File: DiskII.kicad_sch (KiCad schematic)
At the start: 31 parts, among them J1 Apple II Expansion Bus, J2 DRIVE 2, J3 DRIVE 1, Q1 2N3906, Q2 MPSU51, Q3 MPSU51, SW1 A8, SW2 A9, SW3 A10

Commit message: update BOM
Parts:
- J1: now left out of the parts list
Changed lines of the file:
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@@
   )
   (symbol (lib_id "Connector_Generic:Conn_02x25_Counter_Clockwise") (at 64.77 181.61 0) (unit 1)
-    (in_bom yes) (on_board yes)
+    (in_bom no) (on_board yes)
     (property "Reference" "J1" (id 0) (at 66.04 145.6182 0))
     (property "Value" "Apple II Expansion Bus" (id 1) (at 66.04 147.9296 0))

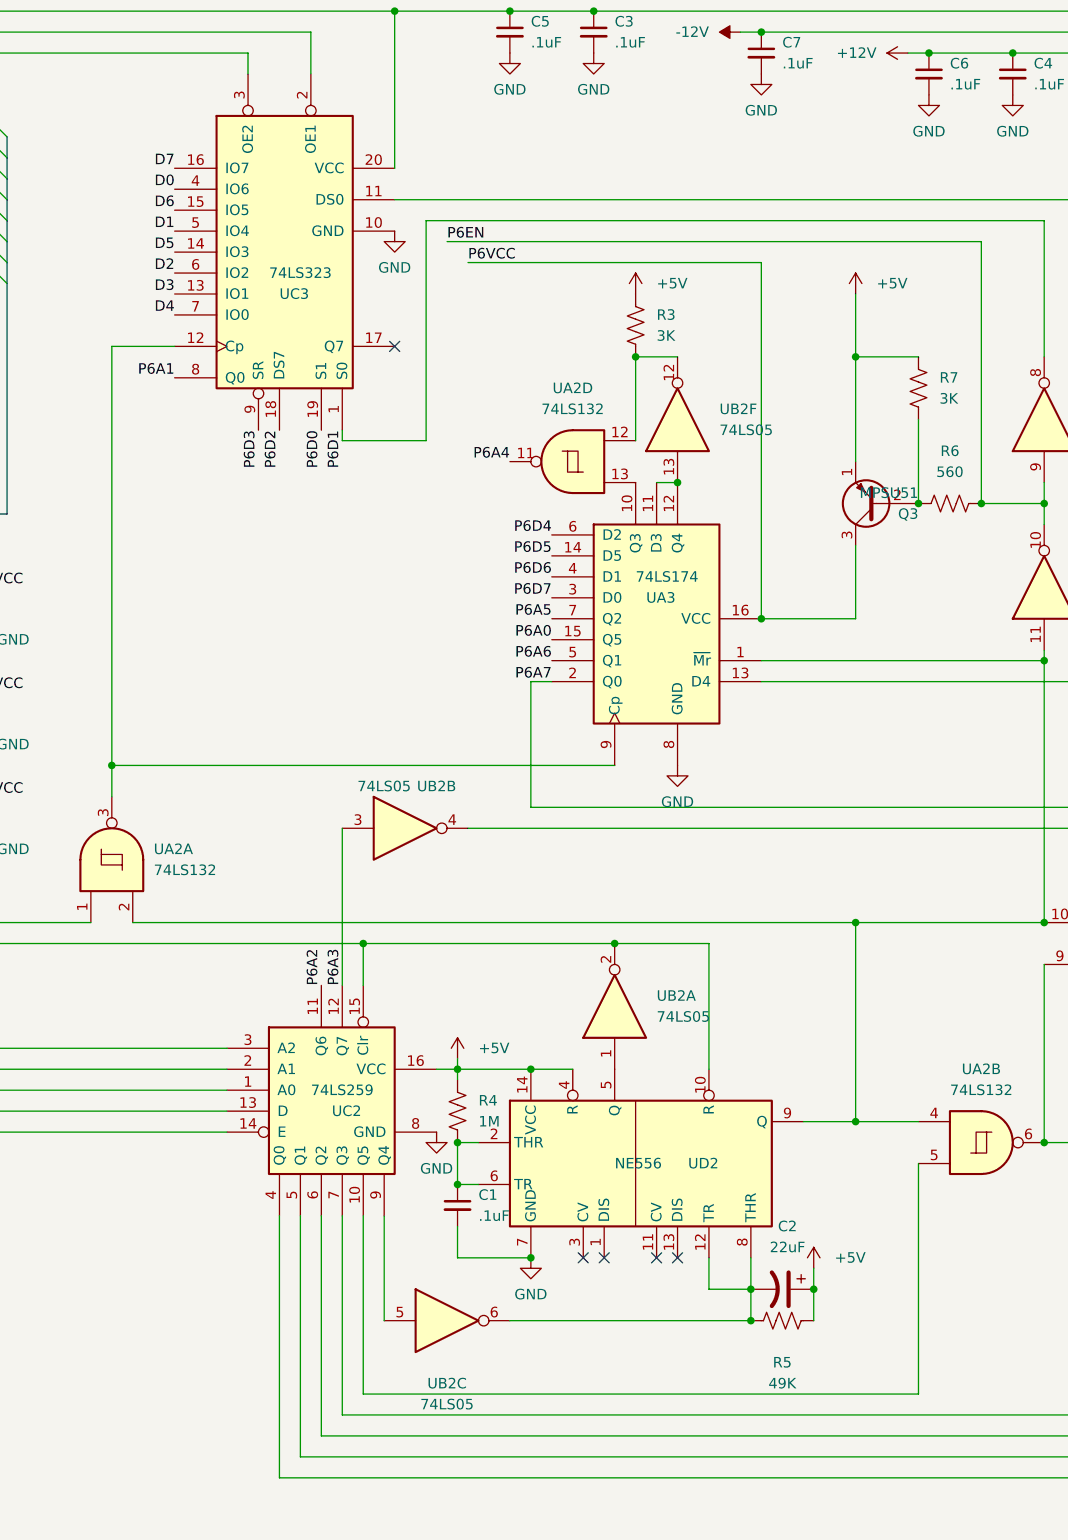
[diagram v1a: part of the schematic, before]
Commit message: fix misrouted data lines to shift register
a few other minor fixes
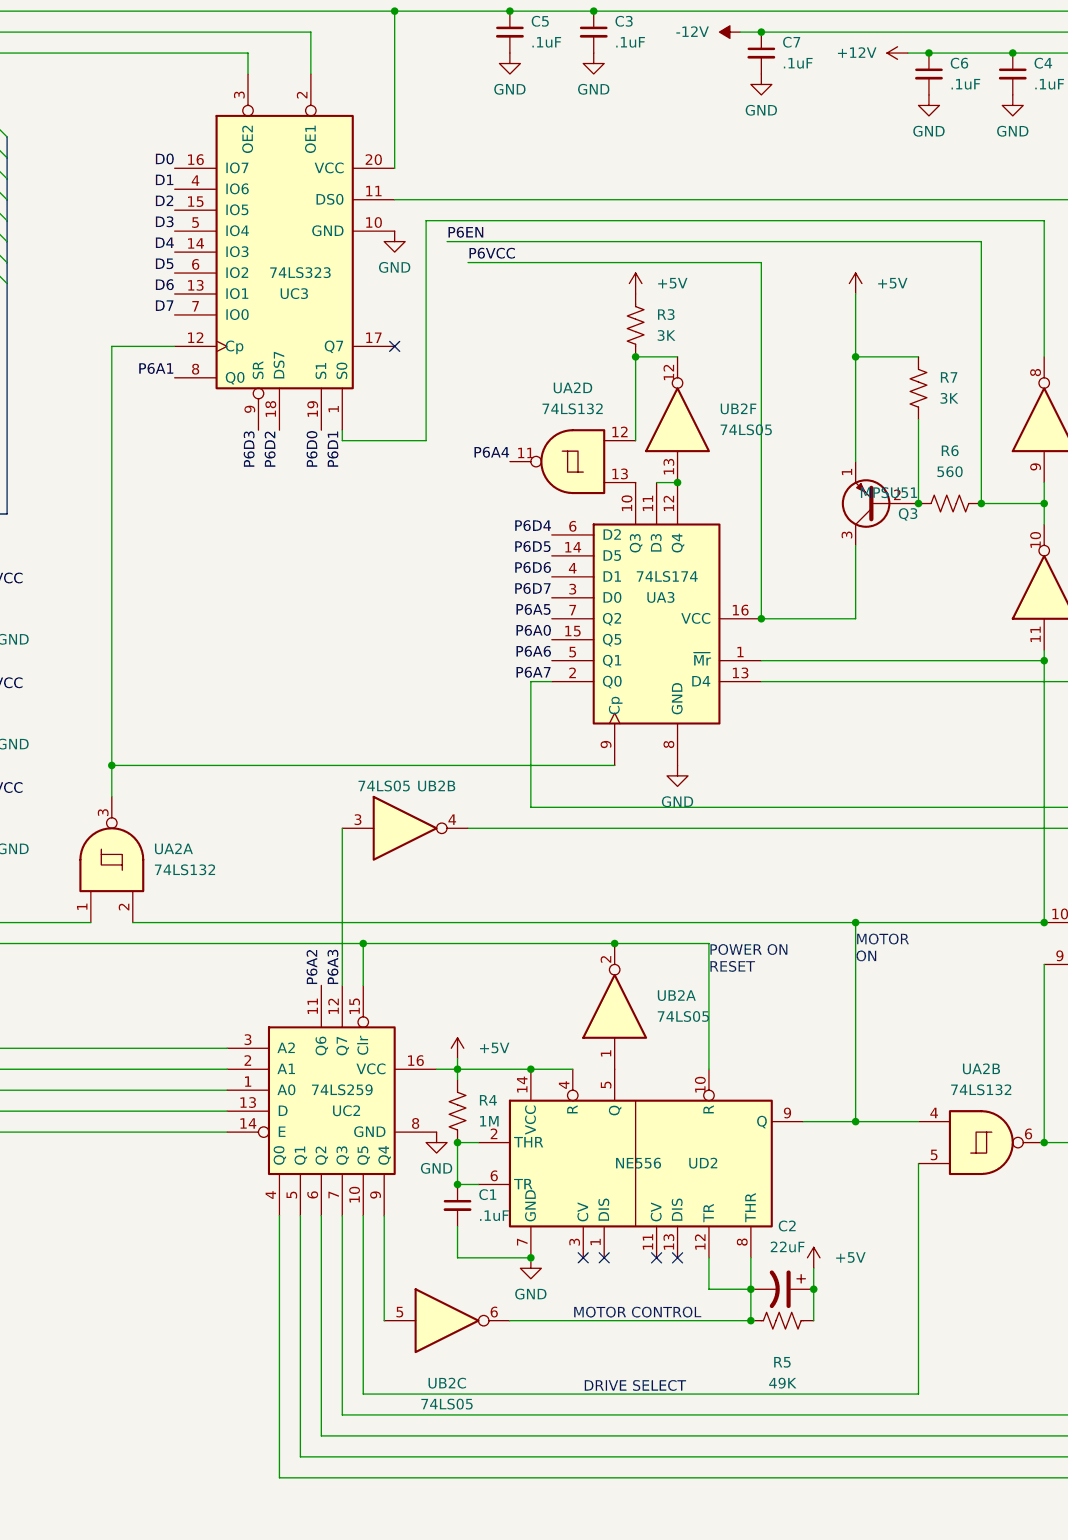
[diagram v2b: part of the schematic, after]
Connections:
- net D0: now also UC3.16 (IO7); no longer UC3.4 (IO6)
- net D1: now also UC3.4 (IO6); no longer UC3.5 (IO4)
- net D2: now also UC3.15 (IO5); no longer UC3.6 (IO2)
- net D3: now also UC3.5 (IO4); no longer UC3.13 (IO1)
- net D4: now also UC3.14 (IO3); no longer UC3.7 (IO0)
- net D5: now also UC3.6 (IO2); no longer UC3.14 (IO3)
- net D6: now also UC3.13 (IO1); no longer UC3.15 (IO5)
- net D7: now also UC3.7 (IO0); no longer UC3.16 (IO7)
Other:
- note added: "DRIVE SELECT"
- note added: "MOTOR CONTROL"
- note added: "MOTOR ON"
- note added: "POWER ON RESET"
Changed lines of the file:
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@@
     (stroke (width 0) (type default) (color 0 0 0 0))
   )
+  (text "MOTOR\nON" (at 234.95 157.48 0)
+    (effects (font (size 1.27 1.27)) (justify left bottom))
+  )
+  (text "POWER ON\nRESET" (at 217.17 158.75 0)
+    (effects (font (size 1.27 1.27)) (justify left bottom))
+  )
+  (text "DRIVE SELECT" (at 201.93 209.55 0)
+    (effects (font (size 1.27 1.27)) (justify left bottom))
+  )
+  (text "MOTOR CONTROL" (at 200.66 200.66 0)
+    (effects (font (size 1.27 1.27)) (justify left bottom))
+  )
   (label "P6A3" (at 54.61 104.14 180)
     (effects (font (size 1.27 1.27)) (justify right bottom))
@@
     (effects (font (size 1.27 1.27)) (justify left bottom))
   )
-  (label "D5" (at 152.4 71.12 180)
+  (label "D5" (at 152.4 73.66 180)
     (effects (font (size 1.27 1.27)) (justify right bottom))
   )
@@
     (effects (font (size 1.27 1.27)) (justify left bottom))
   )
-  (label "D4" (at 152.4 78.74 180)
+  (label "D4" (at 152.4 71.12 180)
     (effects (font (size 1.27 1.27)) (justify right bottom))
   )
@@
     (effects (font (size 1.27 1.27)) (justify left bottom))
   )
-  (label "D7" (at 152.4 60.96 180)
-    (effects (font (size 1.27 1.27)) (justify right bottom))
-  )
-  (label "D3" (at 152.4 76.2 180)
+  (label "D7" (at 152.4 78.74 180)
+    (effects (font (size 1.27 1.27)) (justify right bottom))
+  )
+  (label "D3" (at 152.4 68.58 180)
     (effects (font (size 1.27 1.27)) (justify right bottom))
   )
@@
     (effects (font (size 1.27 1.27)) (justify left bottom))
   )
-  (label "D6" (at 152.4 66.04 180)
-    (effects (font (size 1.27 1.27)) (justify right bottom))
-  )
-  (label "D0" (at 152.4 63.5 180)
+  (label "D6" (at 152.4 76.2 180)
+    (effects (font (size 1.27 1.27)) (justify right bottom))
+  )
+  (label "D0" (at 152.4 60.96 180)
     (effects (font (size 1.27 1.27)) (justify right bottom))
   )
@@
     (effects (font (size 1.27 1.27)) (justify left bottom))
   )
-  (label "D1" (at 152.4 68.58 180)
+  (label "D1" (at 152.4 63.5 180)
     (effects (font (size 1.27 1.27)) (justify right bottom))
   )
@@
     (effects (font (size 1.27 1.27)) (justify left bottom))
   )
-  (label "D2" (at 152.4 73.66 180)
-    (effects (font (size 1.27 1.27)) (justify right bottom))
-  )
+  (label "D2" (at 152.4 66.04 180)
+    (effects (font (size 1.27 1.27)) (justify right bottom))
+  )

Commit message: massive fixups
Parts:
- removed SW2: A9, Connector_PinHeader_2.54mm:PinHeader_2x03_P2.54mm_Vertical, symbol Switch:SW_DPDT_x2
- removed SW3: A10, Connector_PinHeader_2.54mm:PinHeader_2x03_P2.54mm_Vertical, symbol Switch:SW_DPDT_x2
- added JP5A10, JP6A10: A10, Jumper:SolderJumper-3_P1.3mm_Bridged12_RoundedPad1.0x1.5mm_NumberLabels, symbol Jumper:SolderJumper_3_Bridged12
- added JP5A9, JP6A9: A9, Jumper:SolderJumper-3_P1.3mm_Bridged12_RoundedPad1.0x1.5mm_NumberLabels, symbol Jumper:SolderJumper_3_Bridged12
- added unit 2 of UD2
- R1, R2, R3, R6, R7: footprint Resistor_THT:R_Axial_DIN0207_L6.3mm_D2.5mm_P7.62mm_Horizontal -> Resistor_THT:R_Axial_DIN0207_L6.3mm_D2.5mm_P10.16mm_Horizontal
- R4, R5: footprint Resistor_THT:R_Axial_DIN0309_L9.0mm_D3.2mm_P12.70mm_Horizontal -> Resistor_THT:R_Axial_DIN0207_L6.3mm_D2.5mm_P10.16mm_Horizontal
- UB3: value 2758/16 P6 -> 2758/16/32 P6
- UC2: value 74LS259 -> 74LS259/9334
- UD3: value 2758/16 P5 -> 2758/16/32 P5
- renumbered SW1 to SWA8
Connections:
- net +5V: now also UD2.14 (VCC)
- net GND: now also JP5A10.1 (A), JP5A9.1 (A), JP6A10.1 (A), JP6A9.1 (A), UD2.7 (GND)
- net ~{RES}: now also UD2.10 (R); no longer UD2.10 (R)
- net at C2.2, R5.1, UB2.6: now also UD2.12 (THR), UD2.8 (TR); no longer UD2.12 (TR), UD2.8 (THR)
- net at UA2.10, UA2.2, UA2.4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: now also UD2.9 (Q); no longer UD2.9 (Q)
- net P5A10: no longer names the net of UD3.19 (A10)
- net P5A10: now also JP5A10.2 (C)
- net P5A8: no longer names the net of SWA8.2 (B), UD3.23 (A8)
- net P5A9: no longer names the net of UD3.22 (A9)
- net P5A9: now also JP5A9.2 (C)
- net P5VCC: no longer names the net of Q2.3 (C), SWA8.1 (A), UD3.21 (VPP), UD3.24 (VCC)
- net P5VCC: now also JP5A10.3 (B), JP5A9.3 (B)
- net P6A0: no longer names the net of UA3.15 (Q5), UB3.8 (A0)
- net P6A1: no longer names the net of UB3.7 (A1), UC3.8 (Q0)
- net P6A10: no longer names the net of UB3.19 (AR/A10)
- net P6A10: now also JP6A10.2 (C)
- net P6A2: no longer names the net of UB3.6 (A2), UC2.11 (Q6)
- net P6A3: no longer names the net of UB2.3, UB3.5 (A3), UC2.12 (Q7)
- net P6A4: no longer names the net of UA2.11, UB3.4 (A4)
- net P6A5: no longer names the net of UA3.7 (Q2), UB3.3 (A5)
- net P6A6: no longer names the net of UA3.5 (Q1), UB3.2 (A6)
- net P6A7 renamed WR DATA
- net P6A8: no longer names the net of SWA8.5 (B), UB3.23 (A8)
- net P6A9: no longer names the net of UB3.22 (A9)
- net P6A9: now also JP6A9.2 (C)
- net P6D0: no longer names the net of UB3.9 (D0), UC3.19 (S1)
- net P6D1: no longer names the net of UB2.8, UB3.10 (D1), UC3.1 (S0)
- net P6D2: no longer names the net of UB3.11 (D2), UC3.18 (DS7)
- net P6D3: no longer names the net of UB3.13 (D3), UC3.9 (SR)
- net P6D4: no longer names the net of UA3.6 (D2), UB3.14 (D4)
- net P6D5: no longer names the net of UA3.14 (D5), UB3.15 (D5)
- net P6D6: no longer names the net of UA3.4 (D1), UB3.16 (D6)
- net P6D7: no longer names the net of UA3.3 (D0), UB3.17 (D7)
- net P6EN: no longer names the net of R6.2, UB2.10, UB2.9, UB3.18 (~{CE})
- net P6VCC: no longer names the net of Q3.3 (C), SWA8.4 (A), UA3.16 (VCC), UB3.21 (VPP/A11), UB3.24 (VCC)
- net P6VCC: now also JP6A10.3 (B), JP6A9.3 (B)
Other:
- moved on the sheet: C2, C3, C4, C5, C6, C7, J1, J2, J3, Q1, Q2, Q3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

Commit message: revision 1
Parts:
- added JP17: Unidisk, Jumper:SolderJumper-3_P1.3mm_Bridged12_RoundedPad1.0x1.5mm, symbol Jumper:SolderJumper_3_Bridged12
- added JP19: Unidisk, Jumper:SolderJumper-2_P1.3mm_Bridged_RoundedPad1.0x1.5mm, symbol Jumper:SolderJumper_2_Bridged
- J1: value Apple II Expansion Bus -> Apple II Expansion Slot
- Q2, Q3: symbol Transistor_BJT:MPSA92 -> Device:Q_PNP_EBC
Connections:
- net +12V: now also JP17.1 (A), JP19.1 (A); no longer J3.17 (+12), J3.19 (+12)
- net ~{ENBL 2}: now also JP17.3 (B)
- new net: J3.17 (Pin_17), JP17.2 (C)
- new net: J3.19 (Pin_19), JP19.2 (B)
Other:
- moved on the sheet: C1, C2, C3, C4, C5, C6, C7, J1, J2, J3, JP5A10, JP5A9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

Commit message: BOM: no solder jumpers, hide  fab layer by default
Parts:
- JP17, JP19, JP5A10, JP5A9, JP6A10, JP6A9: now left out of the parts list
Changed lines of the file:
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@@
   )
   (symbol (lib_id "Jumper:SolderJumper_3_Bridged12") (at 180.34 165.1 180) (unit 1)
-    (in_bom yes) (on_board yes) (fields_autoplaced)
+    (in_bom no) (on_board yes) (fields_autoplaced)
     (property "Reference" "JP6A10" (id 0) (at 180.34 168.91 0))
     (property "Value" "A10" (id 1) (at 180.34 161.29 0)
@@
   )
   (symbol (lib_id "Jumper:SolderJumper_3_Bridged12") (at 358.14 40.64 90) (mirror x) (unit 1)
-    (in_bom yes) (on_board yes) (fields_autoplaced)
+    (in_bom no) (on_board yes) (fields_autoplaced)
     (property "Reference" "JP17" (id 0) (at 355.6 39.3699 90)
       (effects (font (size 1.27 1.27)) (justify left))
@@
   )
   (symbol (lib_id "Jumper:SolderJumper_2_Bridged") (at 360.68 39.37 90) (mirror x) (unit 1)
-    (in_bom yes) (on_board yes) (fields_autoplaced)
+    (in_bom no) (on_board yes) (fields_autoplaced)
     (property "Reference" "JP19" (id 0) (at 363.22 38.0999 90)
       (effects (font (size 1.27 1.27)) (justify right))
@@
   )
   (symbol (lib_id "Jumper:SolderJumper_3_Bridged12") (at 71.12 88.9 180) (unit 1)
-    (in_bom yes) (on_board yes) (fields_autoplaced)
+    (in_bom no) (on_board yes) (fields_autoplaced)
     (property "Reference" "JP5A9" (id 0) (at 71.12 92.71 0))
     (property "Value" "A9" (id 1) (at 71.12 85.09 0)
@@
   )
   (symbol (lib_id "Jumper:SolderJumper_3_Bridged12") (at 83.82 96.52 180) (unit 1)
-    (in_bom yes) (on_board yes) (fields_autoplaced)
+    (in_bom no) (on_board yes) (fields_autoplaced)
     (property "Reference" "JP5A10" (id 0) (at 83.82 100.33 0))
     (property "Value" "A10" (id 1) (at 83.82 92.71 0)
@@
   )
   (symbol (lib_id "Jumper:SolderJumper_3_Bridged12") (at 167.64 162.56 180) (unit 1)
-    (in_bom yes) (on_board yes) (fields_autoplaced)
+    (in_bom no) (on_board yes) (fields_autoplaced)
     (property "Reference" "JP6A9" (id 0) (at 167.64 166.37 0))
     (property "Value" "A9" (id 1) (at 167.64 158.75 0)
